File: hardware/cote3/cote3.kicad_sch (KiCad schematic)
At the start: 0 parts

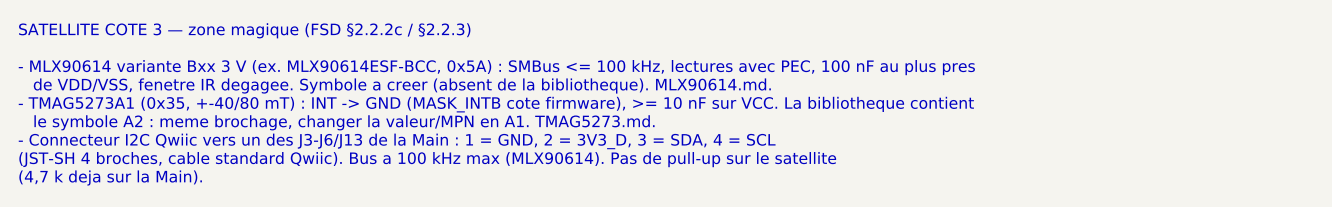
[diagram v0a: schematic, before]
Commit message: docs+bom: MLX90614 retire du produit, Cote 3 = TMAG5273 + proximite capacitive
Cout de la variante 3 V (6,6-8,9 USD), bus I2C bride a 100 kHz. Controleur
tactile de Cote 2 a rechoisir (MTCH2120 sans stock, MPR121 en fin de vie).
Synthese MTCH2120 : boitier REB, motif de pastilles, PDF chiffre.
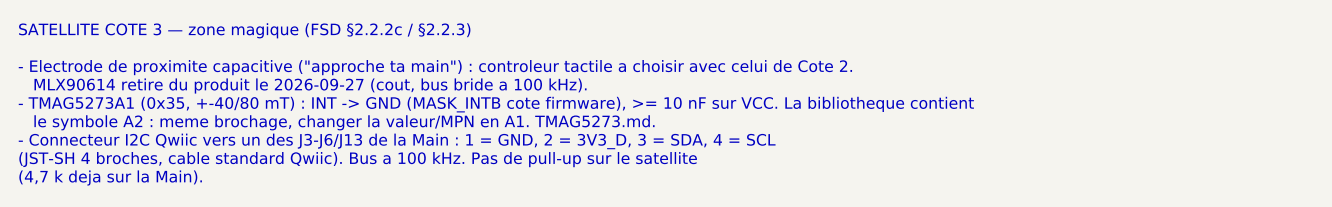
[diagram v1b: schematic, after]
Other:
- note added: "SATELLITE COTE 3 — zone magique (FSD §2.2.2c / §2.2.3) - Electrode de proximite capacitive ("approche ta main") : controleur tactile a choisir avec celui de Cote 2. MLX90614 retire du produit le 2026-09-27 (cout, bus bride a 100 kHz). - TMAG5273A1 (0x35, +-40/80 mT) : INT -> GND (MASK_INTB cote firmware), >= 10 nF sur VCC. La bibliotheque contient le symbole A2 : meme brochage, changer la valeur/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"
- note removed: "SATELLITE COTE 3 — zone magique (FSD §2.2.2c / §2.2.3) - MLX90614 variante Bxx 3 V (ex. MLX90614ESF-BCC, 0x5A) : SMBus <= 100 kHz, lectures avec PEC, 100 nF au plus pres de VDD/VSS, fenetre IR degagee. Symbole a creer (absent de la bibliotheque). MLX90614.md. - TMAG5273A1 (0x35, +-40/80 mT) : INT -> GND (MASK_INTB cote firmware), >= 10 nF sur VCC. La bibliotheque contient le symbole A2 : meme bro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"
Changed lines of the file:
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@@
 	(generator_version "10.0")
 	(paper "A4")
-	(text "SATELLITE COTE 3 — zone magique (FSD §2.2.2c / §2.2.3)\n\n- MLX90614 variante Bxx 3 V (ex. MLX90614ESF-BCC, 0x5A) : SMBus <= 100 kHz, lectures avec PEC, 100 nF au plus pres\n   de VDD/VSS, fenetre IR degagee. Symbole a creer (absent de la bibliotheque). MLX90614.md.\n- TMAG5273A1 (0x35, +-40/80 mT) : INT -> GND (MASK_INTB cote firmware), >= 10 nF sur VCC. La bibliotheque contient\n   le symbole A2 : meme brochage, changer la valeur/MPN en A1. TMAG5273.md.\n- Connecteur I2C Qwiic vers un des J3-J6/J13 de la Main : 1 = GND, 2 = 3V3_D, 3 = SDA, 4 = SCL\n(JST-SH 4 broches, cable standard Qwiic). Bus a 100 kHz max (MLX90614). Pas de pull-up sur le satellite\n(4,7 k deja sur la Main)."
+	(text "SATELLITE COTE 3 — zone magique (FSD §2.2.2c / §2.2.3)\n\n- Electrode de proximite capacitive (\"approche ta main\") : controleur tactile a choisir avec celui de Cote 2.\n   MLX90614 retire du produit le 2026-09-27 (cout, bus bride a 100 kHz).\n- TMAG5273A1 (0x35, +-40/80 mT) : INT -> GND (MASK_INTB cote firmware), >= 10 nF sur VCC. La bibliotheque contient\n   le symbole A2 : meme brochage, changer la valeur/MPN en A1. TMAG5273.md.\n- Connecteur I2C Qwiic vers un des J3-J6/J13 de la Main : 1 = GND, 2 = 3V3_D, 3 = SDA, 4 = SCL\n(JST-SH 4 broches, cable standard Qwiic). Bus a 100 kHz. Pas de pull-up sur le satellite\n(4,7 k deja sur la Main)."
 		(exclude_from_sim no)
 		(at 20.32 142.24 0)

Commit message: hardware+docs: CAP1298 retenu pour le tactile de Cote 2, BOM de reference corrigee (H8)
- Cote 2 : CAP1298-1-SL-TR (C2652072, 8 touches, 0x28 fixe) remplace le MTCH2120
  (aucun stock) ; proximite de Cote 3 en suspens (pas de second CAP12xx).
- BOM : U11 = LSM6DSOXTR, doublon U21 retire, filtre DAC 470 ohm + 2,2 nF C0G,
  TMAG5273A1 (C3716049), U10 SOT-23-6, ecran bouche a choisir, LCSC de D1/Q1/Q2
  dans la bonne colonne, ST25DV et haut-parleur ajoutes.
- docs/pcb/02-bom-lcsc.csv (perimee) supprimee : une seule BOM.
- FSD, RESTE-A-FAIRE, syntheses et cartouches satellites alignes.
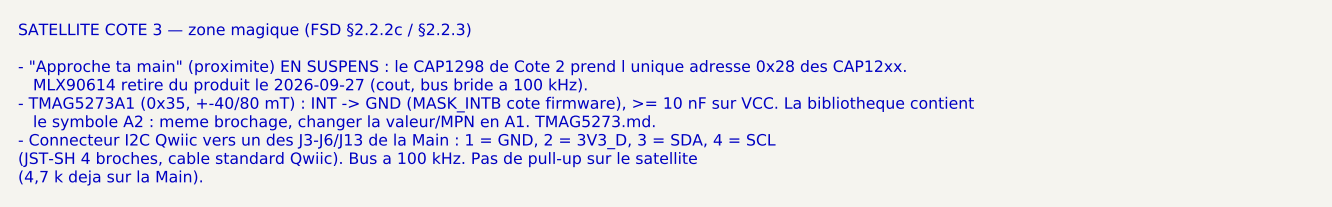
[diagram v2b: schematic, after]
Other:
- note added: "SATELLITE COTE 3 — zone magique (FSD §2.2.2c / §2.2.3) - "Approche ta main" (proximite) EN SUSPENS : le CAP1298 de Cote 2 prend l unique adresse 0x28 des CAP12xx. MLX90614 retire du produit le 2026-09-27 (cout, bus bride a 100 kHz). - TMAG5273A1 (0x35, +-40/80 mT) : INT -> GND (MASK_INTB cote firmware), >= 10 nF sur VCC. La bibliotheque contient le symbole A2 : meme brochage, changer la valeur/MP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"
- note removed: "SATELLITE COTE 3 — zone magique (FSD §2.2.2c / §2.2.3) - Electrode de proximite capacitive ("approche ta main") : controleur tactile a choisir avec celui de Cote 2. MLX90614 retire du produit le 2026-09-27 (cout, bus bride a 100 kHz). - TMAG5273A1 (0x35, +-40/80 mT) : INT -> GND (MASK_INTB cote firmware), >= 10 nF sur VCC. La bibliotheque contient le symbole A2 : meme brochage, changer la valeur/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"
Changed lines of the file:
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@@
 	(generator_version "10.0")
 	(paper "A4")
-	(text "SATELLITE COTE 3 — zone magique (FSD §2.2.2c / §2.2.3)\n\n- Electrode de proximite capacitive (\"approche ta main\") : controleur tactile a choisir avec celui de Cote 2.\n   MLX90614 retire du produit le 2026-09-27 (cout, bus bride a 100 kHz).\n- TMAG5273A1 (0x35, +-40/80 mT) : INT -> GND (MASK_INTB cote firmware), >= 10 nF sur VCC. La bibliotheque contient\n   le symbole A2 : meme brochage, changer la valeur/MPN en A1. TMAG5273.md.\n- Connecteur I2C Qwiic vers un des J3-J6/J13 de la Main : 1 = GND, 2 = 3V3_D, 3 = SDA, 4 = SCL\n(JST-SH 4 broches, cable standard Qwiic). Bus a 100 kHz. Pas de pull-up sur le satellite\n(4,7 k deja sur la Main)."
+	(text "SATELLITE COTE 3 — zone magique (FSD §2.2.2c / §2.2.3)\n\n- \"Approche ta main\" (proximite) EN SUSPENS : le CAP1298 de Cote 2 prend l unique adresse 0x28 des CAP12xx.\n   MLX90614 retire du produit le 2026-09-27 (cout, bus bride a 100 kHz).\n- TMAG5273A1 (0x35, +-40/80 mT) : INT -> GND (MASK_INTB cote firmware), >= 10 nF sur VCC. La bibliotheque contient\n   le symbole A2 : meme brochage, changer la valeur/MPN en A1. TMAG5273.md.\n- Connecteur I2C Qwiic vers un des J3-J6/J13 de la Main : 1 = GND, 2 = 3V3_D, 3 = SDA, 4 = SCL\n(JST-SH 4 broches, cable standard Qwiic). Bus a 100 kHz. Pas de pull-up sur le satellite\n(4,7 k deja sur la Main)."
 		(exclude_from_sim no)
 		(at 20.32 142.24 0)

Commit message: hardware(cote2): partie tactile CAP1298 dessinee, approche ta main sur Cote 2
- U2 CAP1298 (0x28), C1 100 nF + C2 1 uF (figure 3-1), J3 Qwiic, ALERT# et N/C a GND.
- 6 touches (CS1-4, CS6, CS7), proximite CS8 gardee par SG (CS5), electrodes
  E1-E8 sur le PCB (TestPoint provisoires, hors BOM). Netlist verifiee.
- Cote 3 = TMAG5273 seul. Bibliotheque : CAP1298 importe, MLX90614 et
  MTCH2120 retires. BOM, FSD, RESTE-A-FAIRE et synthese CAP1298 alignes.
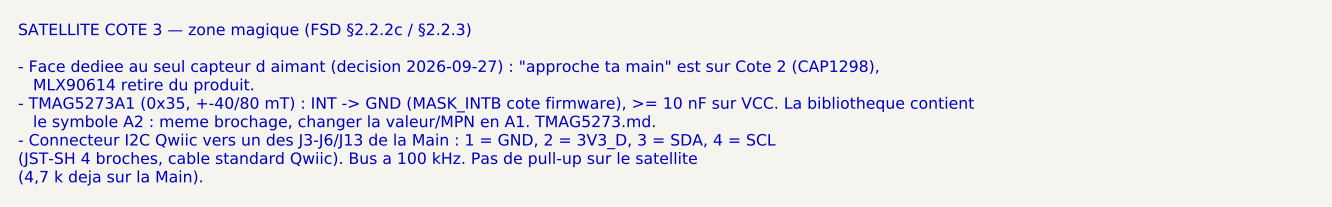
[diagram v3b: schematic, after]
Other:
- note added: "SATELLITE COTE 3 — zone magique (FSD §2.2.2c / §2.2.3) - Face dediee au seul capteur d aimant (decision 2026-09-27) : "approche ta main" est sur Cote 2 (CAP1298), MLX90614 retire du produit. - TMAG5273A1 (0x35, +-40/80 mT) : INT -> GND (MASK_INTB cote firmware), >= 10 nF sur VCC. La bibliotheque contient le symbole A2 : meme brochage, changer la valeur/MPN en A1. TMAG5273.md. - Connecteur I2C Qwi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"
- note removed: "SATELLITE COTE 3 — zone magique (FSD §2.2.2c / §2.2.3) - "Approche ta main" (proximite) EN SUSPENS : le CAP1298 de Cote 2 prend l unique adresse 0x28 des CAP12xx. MLX90614 retire du produit le 2026-09-27 (cout, bus bride a 100 kHz). - TMAG5273A1 (0x35, +-40/80 mT) : INT -> GND (MASK_INTB cote firmware), >= 10 nF sur VCC. La bibliotheque contient le symbole A2 : meme brochage, changer la valeur/MP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"
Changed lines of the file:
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@@
 	(generator_version "10.0")
 	(paper "A4")
-	(text "SATELLITE COTE 3 — zone magique (FSD §2.2.2c / §2.2.3)\n\n- \"Approche ta main\" (proximite) EN SUSPENS : le CAP1298 de Cote 2 prend l unique adresse 0x28 des CAP12xx.\n   MLX90614 retire du produit le 2026-09-27 (cout, bus bride a 100 kHz).\n- TMAG5273A1 (0x35, +-40/80 mT) : INT -> GND (MASK_INTB cote firmware), >= 10 nF sur VCC. La bibliotheque contient\n   le symbole A2 : meme brochage, changer la valeur/MPN en A1. TMAG5273.md.\n- Connecteur I2C Qwiic vers un des J3-J6/J13 de la Main : 1 = GND, 2 = 3V3_D, 3 = SDA, 4 = SCL\n(JST-SH 4 broches, cable standard Qwiic). Bus a 100 kHz. Pas de pull-up sur le satellite\n(4,7 k deja sur la Main)."
+	(text "SATELLITE COTE 3 — zone magique (FSD §2.2.2c / §2.2.3)\n\n- Face dediee au seul capteur d aimant (decision 2026-09-27) : \"approche ta main\" est sur Cote 2 (CAP1298),\n   MLX90614 retire du produit.\n- TMAG5273A1 (0x35, +-40/80 mT) : INT -> GND (MASK_INTB cote firmware), >= 10 nF sur VCC. La bibliotheque contient\n   le symbole A2 : meme brochage, changer la valeur/MPN en A1. TMAG5273.md.\n- Connecteur I2C Qwiic vers un des J3-J6/J13 de la Main : 1 = GND, 2 = 3V3_D, 3 = SDA, 4 = SCL\n(JST-SH 4 broches, cable standard Qwiic). Bus a 100 kHz. Pas de pull-up sur le satellite\n(4,7 k deja sur la Main)."
 		(exclude_from_sim no)
 		(at 20.32 142.24 0)

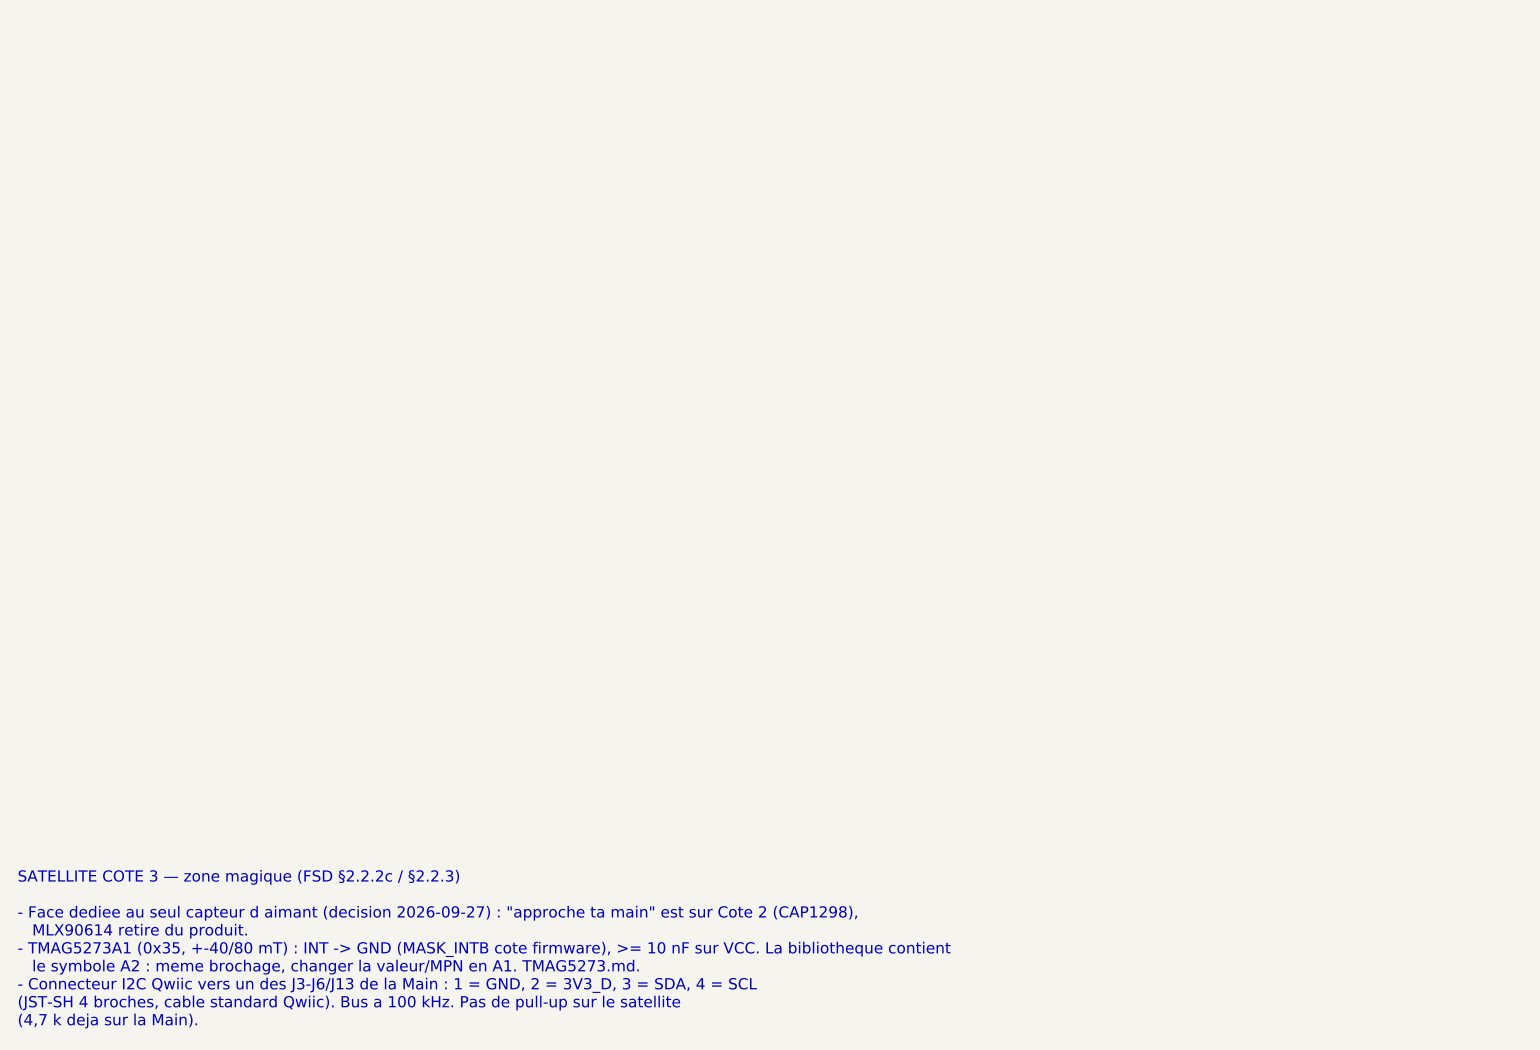
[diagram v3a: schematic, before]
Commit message: hardware: schemas des satellites Dessus, Devant, Cote 1 et Cote 3
- Dessus : ST25DV04KC (10 nF + 100 nF), antenne boucle ANT1 (~4,8 uH, empreinte a creer), accord C3 DNP, Qwiic
- Devant : BMP280 (CSB sur VDDIO, SDO GND), VEML7700, liaisons J7/J7b/J9, embases yeux/bouche provisoires, halo 8 WS2812B
- Cote 1 : ADS7830 ratiometrique, 4 faders PTA6043, 4 pots PDB181, liaison J8, toggles/boutons en facade sur JST-PH
- Cote 3 : TMAG5273A1 (INT et TEST a GND), 100 nF, Qwiic
- BOM : lignes satellites prefixees par face, recoupees avec les schemas
- Brochages corriges dans les syntheses : ST25DV (1 V_EH, 2 AC0) et VEML7700 (2 VDD, 4 SDA)
- Questions ouvertes : docs/audits/2026-09-27-questions-satellites.md
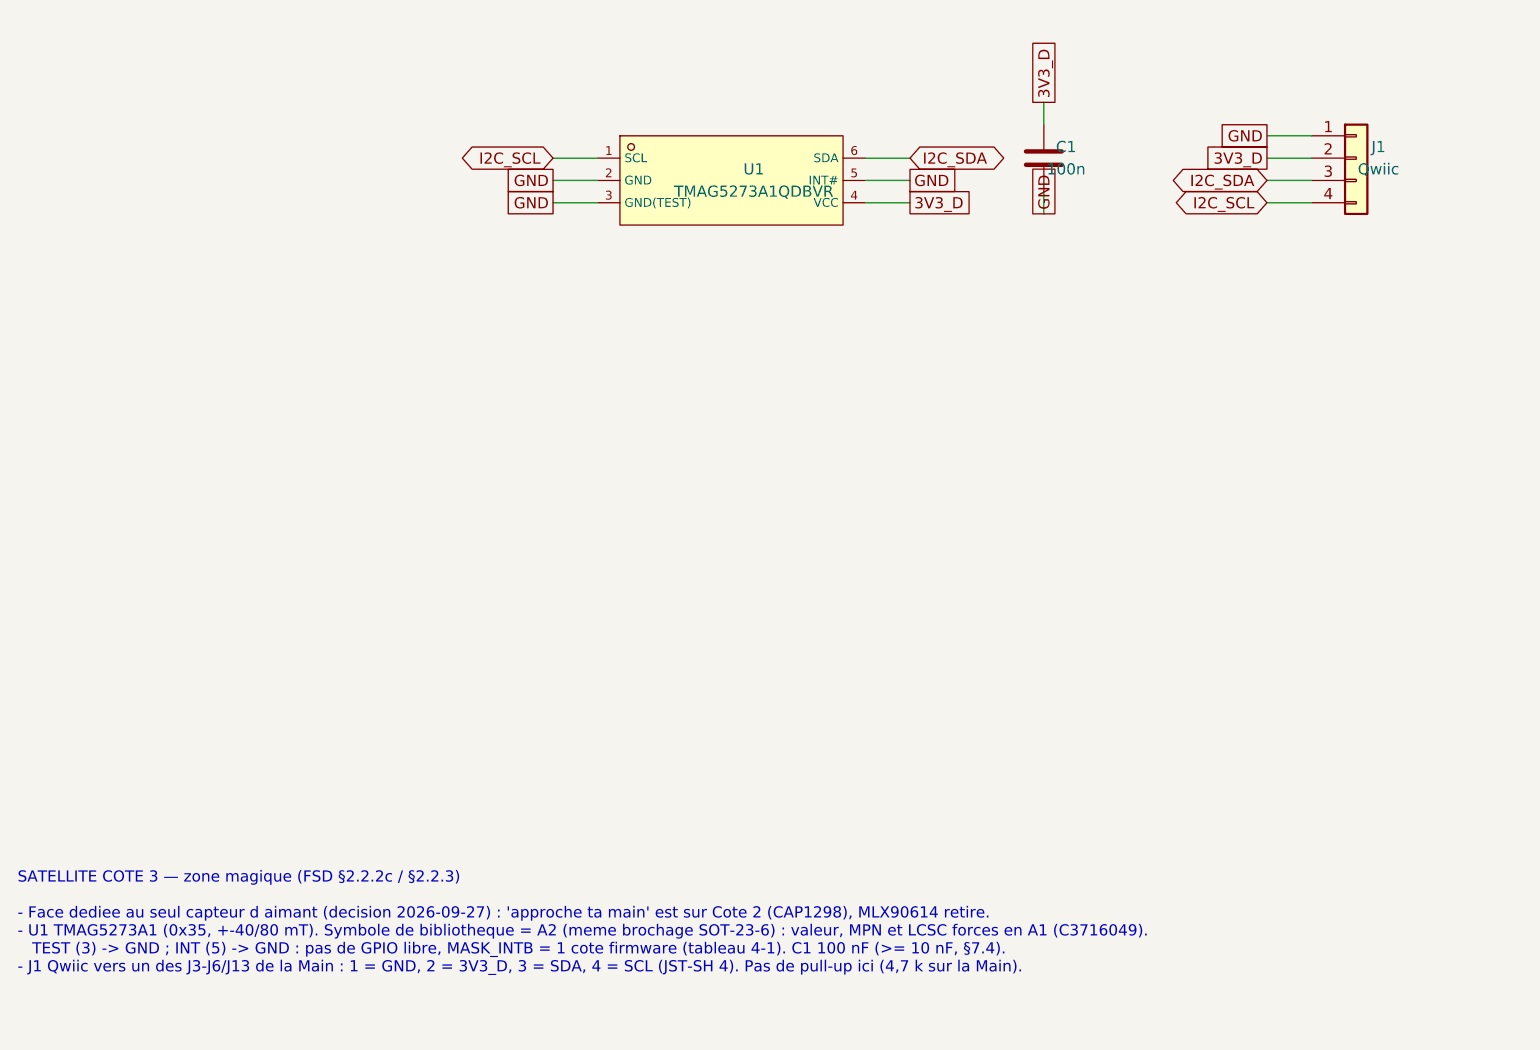
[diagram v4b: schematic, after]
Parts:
- added C1: 100n, Capacitor_SMD:C_0402_1005Metric, symbol Device:C
- added J1: Qwiic, Connector_JST:JST_SH_BM04B-SRSS-TB_1x04-1MP_P1.00mm_Vertical, symbol Connector_Generic:Conn_01x04
- added U1: TMAG5273A1QDBVR, lcsc_footprints:C3715882_SOT-23-6_L2_9-W1_6-P0_95-LS2_8-BR, symbol lcsc_imported:TMAG5273A2QDBVR
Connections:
- new net 3V3_D: C1.1, J1.2 (Pin_2), U1.4 (VCC)
- new net GND: C1.2, J1.1 (Pin_1), U1.2 (GND), U1.3 (GND(TEST)), U1.5 (INT#)
- new net I2C_SCL: J1.4 (Pin_4), U1.1 (SCL)
- new net I2C_SDA: J1.3 (Pin_3), U1.6 (SDA)
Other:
- note added: "SATELLITE COTE 3 — zone magique (FSD §2.2.2c / §2.2.3) - Face dediee au seul capteur d aimant (decision 2026-09-27) : 'approche ta main' est sur Cote 2 (CAP1298), MLX90614 retire. - U1 TMAG5273A1 (0x35, +-40/80 mT). Symbole de bibliotheque = A2 (meme brochage SOT-23-6) : valeur, MPN et LCSC forces en A1 (C3716049). TEST (3) -> GND ; INT (5) -> GND : pas de GPIO libre, MASK_INTB = 1 cote firmware 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"
- note removed: "SATELLITE COTE 3 — zone magique (FSD §2.2.2c / §2.2.3) - Face dediee au seul capteur d aimant (decision 2026-09-27) : "approche ta main" est sur Cote 2 (CAP1298), MLX90614 retire du produit. - TMAG5273A1 (0x35, +-40/80 mT) : INT -> GND (MASK_INTB cote firmware), >= 10 nF sur VCC. La bibliotheque contient le symbole A2 : meme brochage, changer la valeur/MPN en A1. TMAG5273.md. - Connecteur I2C Qwi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"
